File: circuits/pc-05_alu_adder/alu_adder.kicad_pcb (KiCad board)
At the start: 2 copper layers, 99.1 x 99.1 mm, 7 parts, among them J1 Conn_01x10

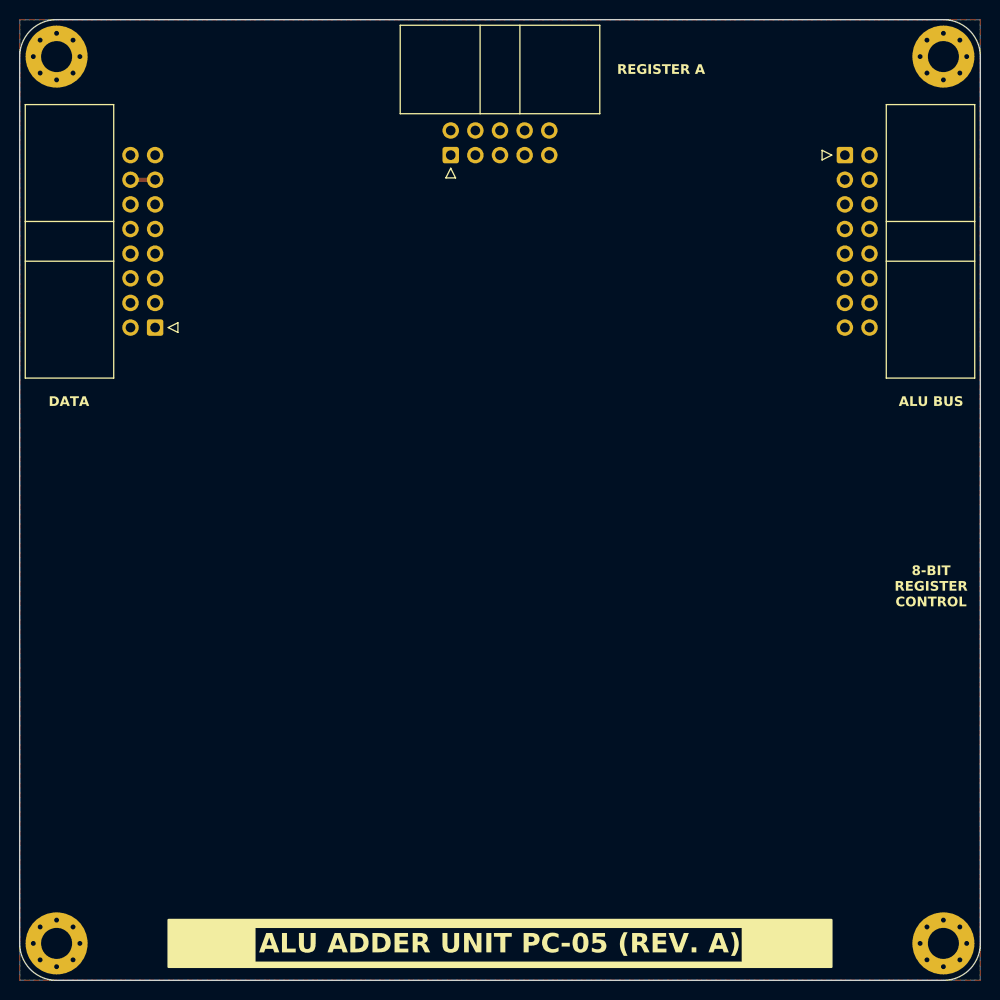
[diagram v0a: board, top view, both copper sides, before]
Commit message: pc-05: ALU adder prototype
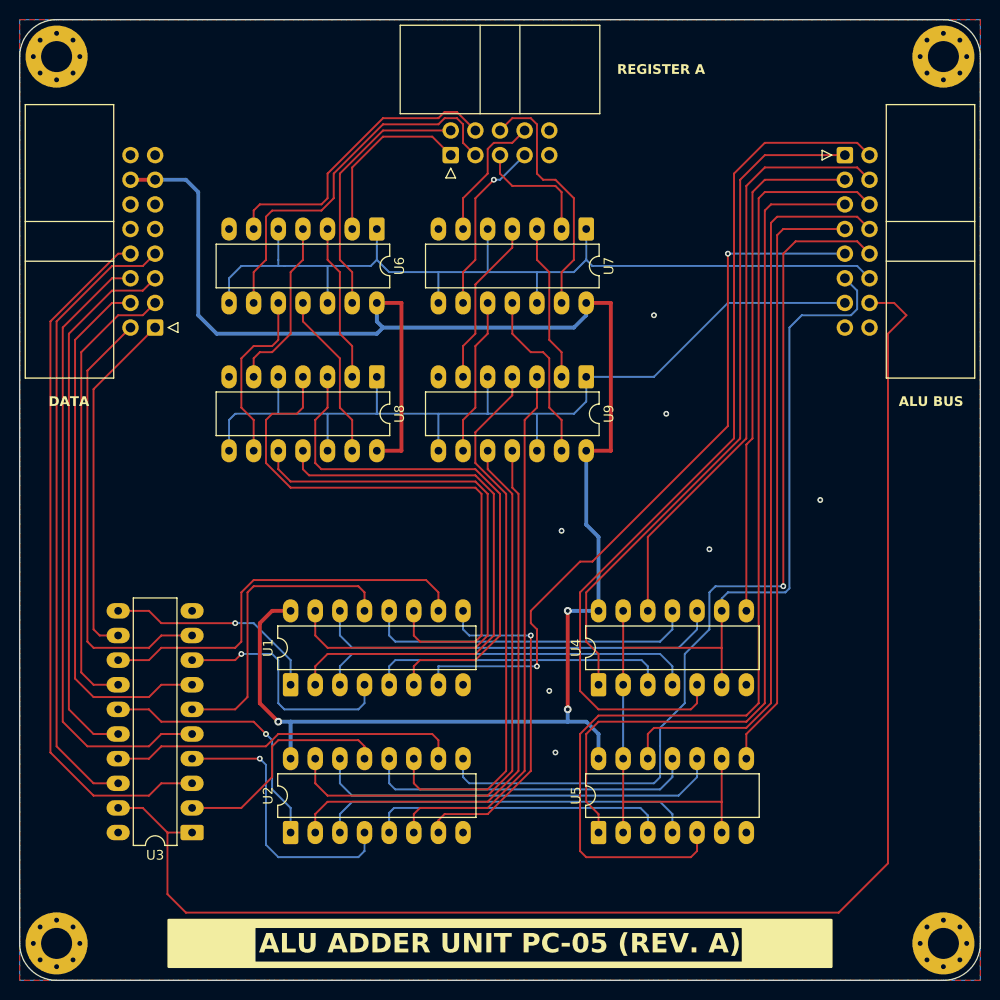
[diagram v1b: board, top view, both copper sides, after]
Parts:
- added U1: 74LS283, Package_DIP:DIP-16_W7.62mm_LongPads, F.Cu at (68.6, 91.4)
- added U2: 74LS283, Package_DIP:DIP-16_W7.62mm_LongPads, F.Cu at (68.6, 106.7)
- added U3: 74AHC244, Package_DIP:DIP-20_W7.62mm_LongPads, F.Cu at (58.4, 106.7)
- added U4: 4070, Package_DIP:DIP-14_W7.62mm_LongPads, F.Cu at (100.3, 91.4)
- added U5: 4070, Package_DIP:DIP-14_W7.62mm_LongPads, F.Cu at (100.3, 106.7)
- added U6: 4081, Package_DIP:DIP-14_W7.62mm_LongPads, F.Cu at (77.5, 44.5)
- added U7: 4081, Package_DIP:DIP-14_W7.62mm_LongPads, F.Cu at (99.1, 44.5)
- added U8: 4071, Package_DIP:DIP-14_W7.62mm_LongPads, F.Cu at (77.5, 59.7)
- added U9: 4071, Package_DIP:DIP-14_W7.62mm_LongPads, F.Cu at (99.1, 59.7)
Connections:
- net /adr14 renamed /~{logic_out}
- ADDRESS_BUS1 pad 1: /adr0 -> /input0
- ADDRESS_BUS1 pad 10: /adr9 -> /adder_carry_out
- ADDRESS_BUS1 pad 11: /adr10 -> /cmd0
- ADDRESS_BUS1 pad 12: /adr11 -> /cmd1
- ADDRESS_BUS1 pad 13: /adr12 -> /cmd2
- ADDRESS_BUS1 pad 14: /adr13 -> /~{adder_out}
- ADDRESS_BUS1 pad 16: /adr15 -> unconnected-(ADDRESS_BUS1-Pin_16-Pad16)
- ADDRESS_BUS1 pad 2: /adr1 -> /input1
- ADDRESS_BUS1 pad 3: /adr2 -> /input2
- ADDRESS_BUS1 pad 4: /adr3 -> /input3
- ADDRESS_BUS1 pad 5: /adr4 -> /input4
- ADDRESS_BUS1 pad 6: /adr5 -> /input5
- ADDRESS_BUS1 pad 7: /adr6 -> /input6
- ADDRESS_BUS1 pad 8: /adr7 -> /input7
- ADDRESS_BUS1 pad 9: /adr8 -> /carry_in
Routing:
- net VCC: track 2.54 -> 192.7 mm, vias 0 -> 3
- net /~{adder_out}: track 0.00 -> 153.9 mm
- net /input5: track 0.00 -> 110.6 mm
- net /cmd0: track 0.00 -> 105.5 mm
- net /cmd2: track 0.00 -> 96.0 mm
- net /adder_carry_out: track 0.00 -> 96.0 mm, vias 0 -> 1
- net /cmd1: track 0.00 -> 96.0 mm
- net /input1: track 0.00 -> 90.7 mm
- net /input4: track 0.00 -> 89.7 mm
- net /input7: track 0.00 -> 77.0 mm
- net /carry_in: track 0.00 -> 76.1 mm, vias 0 -> 2
- net /data7: track 0.00 -> 72.6 mm
- net /input0: track 0.00 -> 71.0 mm
- net /data6: track 0.00 -> 64.8 mm
- net /data5: track 0.00 -> 64.6 mm
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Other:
- board text removed: "8-BIT REGISTER CONTROL"

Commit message: pc-05: polishing of adder circuit
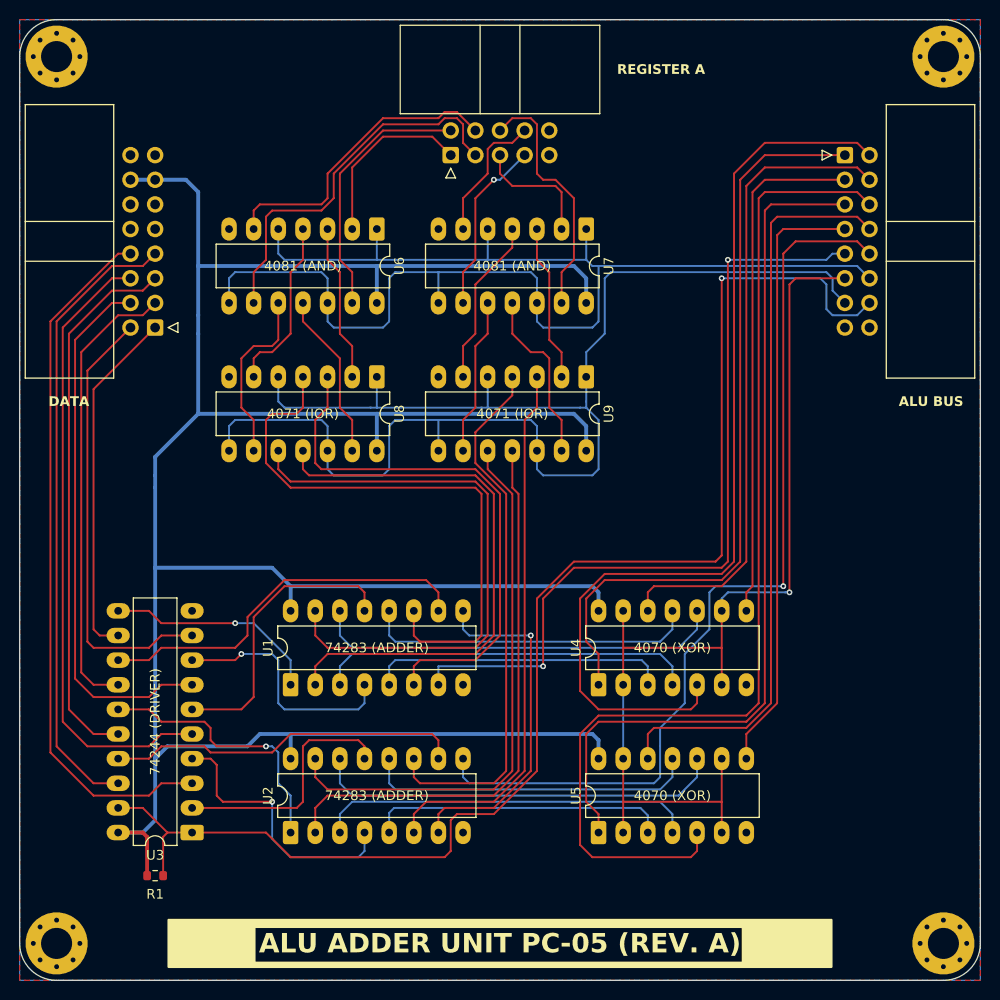
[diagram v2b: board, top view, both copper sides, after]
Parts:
- added R1: 100k, Resistor_SMD:R_0603_1608Metric, F.Cu at (54.6, 111.1)
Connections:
- U3 pad 10: unconnected-(U3-GND-Pad10) -> GND
- U3 pad 20: unconnected-(U3-VCC-Pad20) -> VCC
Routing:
- net VCC: track 192.7 -> 282.1 mm, vias 3 -> 0
- net /cmd2: track 96.0 -> 148.2 mm
- net /cmd1: track 96.0 -> 139.0 mm
- net /~{adder_out}: track 153.9 -> 141.5 mm, vias 0 -> 1
- net /carry_in: track 76.1 -> 83.8 mm
- net /input1: track 90.7 -> 97.8 mm
- net /input0: track 71.0 -> 78.1 mm
- net /input3: track 62.0 -> 66.1 mm
- net /sum3: track 41.8 -> 40.0 mm
- net /sum6: track 24.1 -> 25.6 mm
- net /sum2: track 31.5 -> 30.0 mm
- net /adder_b7: track 56.7 -> 55.8 mm
- net /adder_b6: track 58.5 -> 57.6 mm
- net /cmd0: track 105.5 -> 104.7 mm, vias 0 -> 1
- net /sum4: track 29.0 -> 28.2 mm
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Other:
- board text added: "4070 (XOR)"
- board text added: "4071 (IOR)"
- board text added: "4081 (AND)"
- board text added: "74244 (DRIVER)"
- board text added: "74283 (ADDER)"

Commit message: add filter and decoupling capacitors to all boards
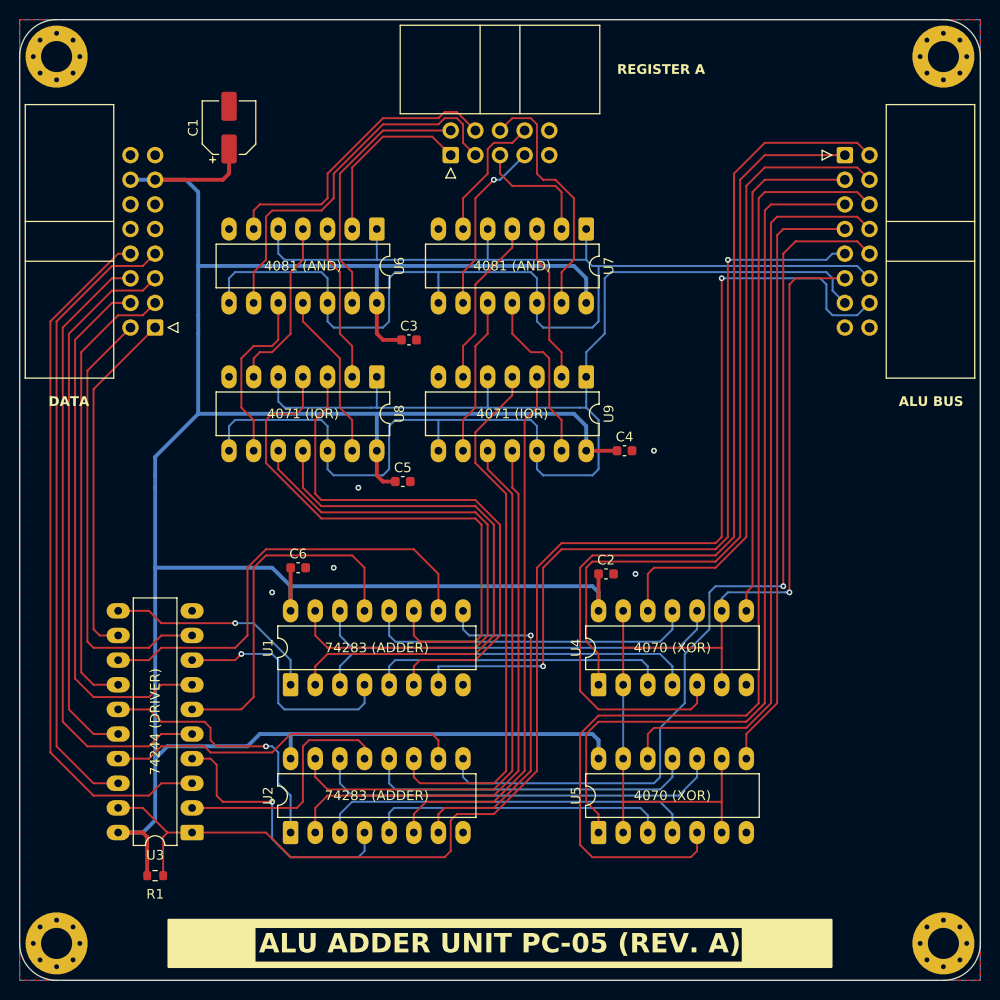
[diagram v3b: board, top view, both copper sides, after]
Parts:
- added C1: C_Polarized, Capacitor_SMD:CP_Elec_5x5.3, F.Cu at (62.2, 34.0)
- added C2: C, Capacitor_SMD:C_0603_1608Metric, F.Cu at (101.1, 80.0)
- added C3: C, Capacitor_SMD:C_0603_1608Metric, F.Cu at (80.8, 55.9)
- added C4: C, Capacitor_SMD:C_0603_1608Metric, F.Cu at (103.0, 67.3)
- added C5: C, Capacitor_SMD:C_0603_1608Metric, F.Cu at (80.2, 70.5)
- added C6: C, Capacitor_SMD:C_0603_1608Metric, F.Cu at (69.4, 79.4)
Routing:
- net VCC: track 282.1 -> 314.6 mm
- net /sum2: track 30.0 -> 37.1 mm
- net /sum3: track 40.0 -> 46.7 mm
- net /adder_b3: track 60.2 -> 58.3 mm
- net /adder_b2: track 60.5 -> 58.7 mm
- net /~{adder_out}: track 141.5 -> 142.3 mm
- net /adder_b1: track 58.9 -> 58.1 mm
- net GND: vias 0 -> 5
